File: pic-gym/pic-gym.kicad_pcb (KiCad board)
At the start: 2 copper layers, 63.5 x 55 mm, 30 parts, among them CON1 BARREL_JACK, SW1 SW_SPST, SW2 SW_Push, SW3 SW_DIP_x05, U1 LM7805, U2 PIC16F84A-XX/P, Y1 4MHz

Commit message: Layout in process
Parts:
- moved U1 3.04 mm to (141.0, 108.0)
- moved D1 0.50 mm to (136.0, 124.5)
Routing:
- net Net-(D5-Pad2): track 0.00 -> 108.7 mm
- net Net-(D4-Pad2): track 0.00 -> 96.8 mm
- net Net-(D7-Pad2): track 0.00 -> 84.2 mm, vias 0 -> 4
- net Net-(D9-Pad2): track 0.00 -> 81.0 mm, vias 0 -> 1
- net Net-(D6-Pad2): track 0.00 -> 76.5 mm, vias 0 -> 2
- net +5V: track 0.00 -> 75.8 mm, vias 0 -> 1
- net Net-(D3-Pad2): track 0.00 -> 70.6 mm, vias 0 -> 1
- net GND: track 0.00 -> 66.4 mm
- net Net-(RN2-Pad2): track 0.00 -> 62.0 mm, vias 0 -> 5
- net Net-(D8-Pad2): track 0.00 -> 55.2 mm, vias 0 -> 2
- net Net-(RN2-Pad5): track 0.00 -> 52.9 mm, vias 0 -> 3
- net Net-(D10-Pad2): track 0.00 -> 51.4 mm, vias 0 -> 3
- net Net-(D1-Pad2): track 0.00 -> 40.6 mm
- net Net-(C3-Pad1): track 0.00 -> 38.2 mm, vias 0 -> 1
- net Net-(RN2-Pad6): track 0.00 -> 37.4 mm, vias 0 -> 2
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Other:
- outline, holes or cut-outs redrawn
- net class 0.2mm added: clearance 0.2, trace_width 0.2, via_dia 0.6858, via_drill 0.3302
- net class Default: clearance 0.2 -> 0.254; trace_width 0.25 -> 0.254; via_dia 0.6 -> 0.6858; via_drill 0.4 -> 0.3302
- net class minimal added: clearance 0.1524, trace_width 0.1524, via_dia 0.6858, via_drill 0.3302
- rule trace_clearance: 0.2 -> 0.254
- rule trace_min: 0.2 -> 0.1524
- rule via_min_drill: 0.3 -> 0.3302
- rule via_min_size: 0.4 -> 0.6858

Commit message: Routed Board
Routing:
- net GND: track 66.4 -> 134.9 mm, vias 0 -> 5
- net Net-(D8-Pad2): track 55.2 -> 117.5 mm, vias 2 -> 4
- net Net-(D9-Pad2): track 81.0 -> 114.7 mm
- net Net-(AFF1-Pad9): track 0.00 -> 5.51 mm, vias 0 -> 1
- net Net-(D4-Pad2): track 96.8 -> 93.8 mm
- net Net-(AFF1-Pad5): track 27.3 -> 28.0 mm
- added copper zone on B.Cu, net GND
- added copper zone on F.Cu, net GND

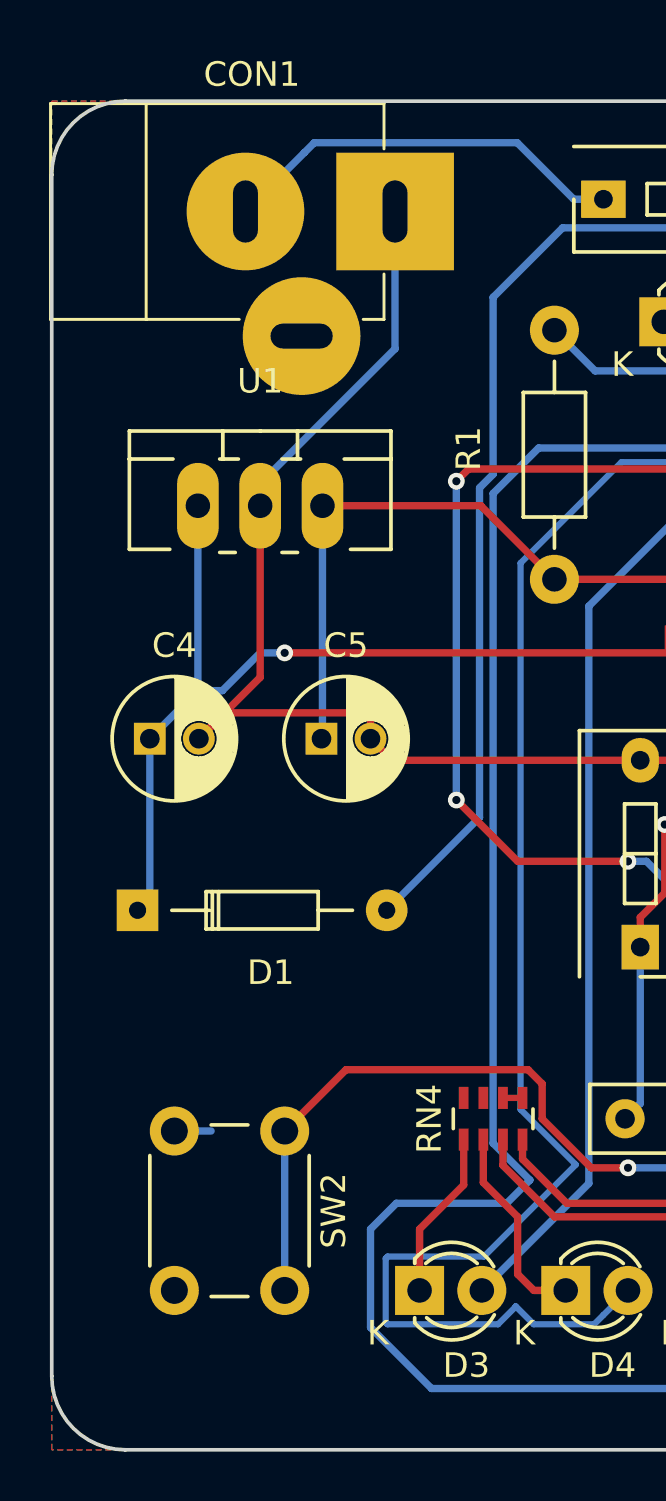
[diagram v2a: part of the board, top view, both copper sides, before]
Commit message: Silkscreen added
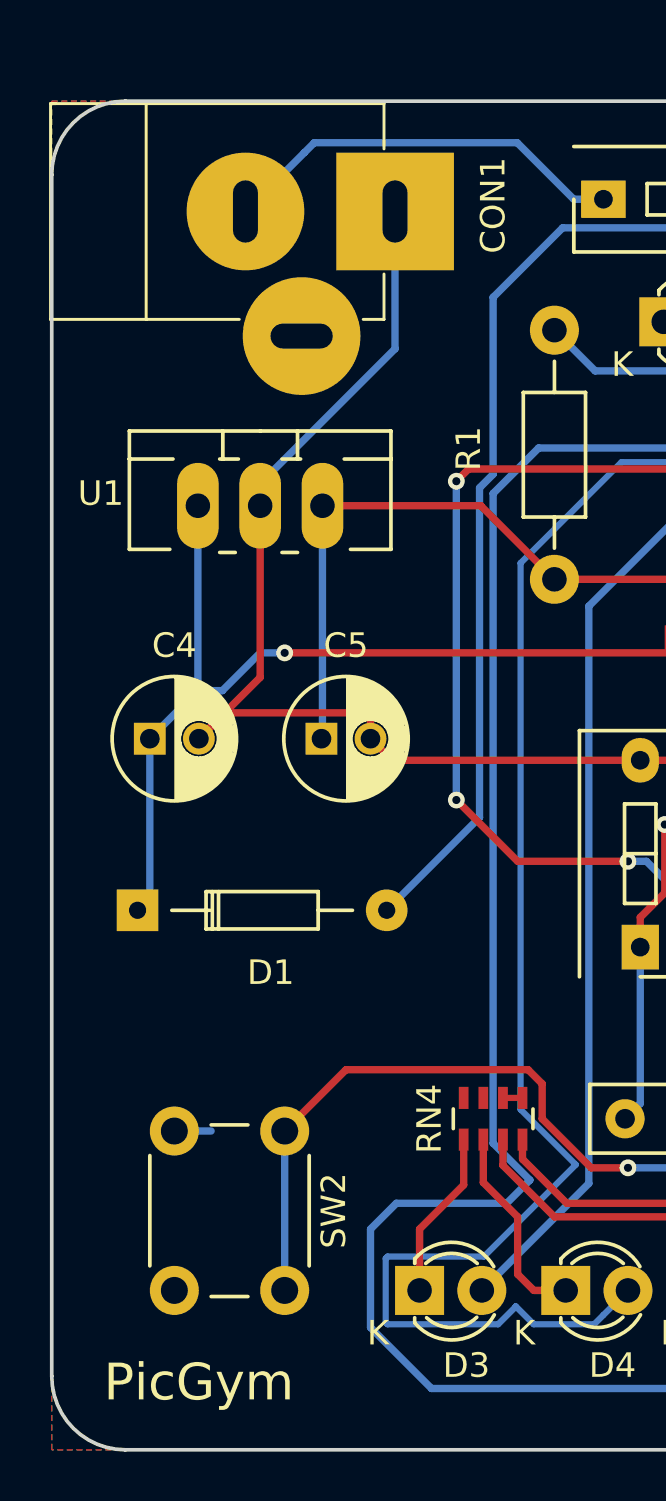
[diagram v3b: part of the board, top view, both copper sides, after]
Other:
- board text added: "D.Matias - 2017"
- board text added: "PicGym"
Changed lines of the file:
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@@
     (area 132.424999 91.424999 196.075001 146.575001)
     (thickness 1.6)
-    (drawings 8)
+    (drawings 10)
     (tracks 498)
     (zones 0)
@@
     (descr "module 1 pin (ou trou mecanique de percage)")
     (tags "CONN JACK")
-    (fp_text reference CON1 (at -5.84 -5.59) (layer F.SilkS)
+    (fp_text reference CON1 (at 4 -0.25 90) (layer F.SilkS)
       (effects (font (size 1 1) (thickness 0.15)))
     )
@@
     (descr "TO-220, Neutral, Vertical, Large Pads,")
     (tags "TO-220, Neutral, Vertical, Large Pads,")
-    (fp_text reference U1 (at 0 -5.08) (layer F.SilkS)
+    (fp_text reference U1 (at -6.5 -0.5) (layer F.SilkS)
       (effects (font (size 1 1) (thickness 0.15)))
     )
@@
     )
   )
+  (gr_text "D.Matias - 2017" (at 184 94) (layer B.SilkS)
+    (effects (font (size 1.5 1.5) (thickness 0.3)) (justify mirror))
+  )
+  (gr_text PicGym (at 138.5 143.75) (layer F.SilkS)
+    (effects (font (size 1.5 1.5) (thickness 0.3)))
+  )
   (gr_line (start 132.5 94.5) (end 132.5 143.5) (layer Edge.Cuts) (width 0.15))
